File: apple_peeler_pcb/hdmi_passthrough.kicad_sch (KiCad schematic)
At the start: 2 parts, among them U3 4066

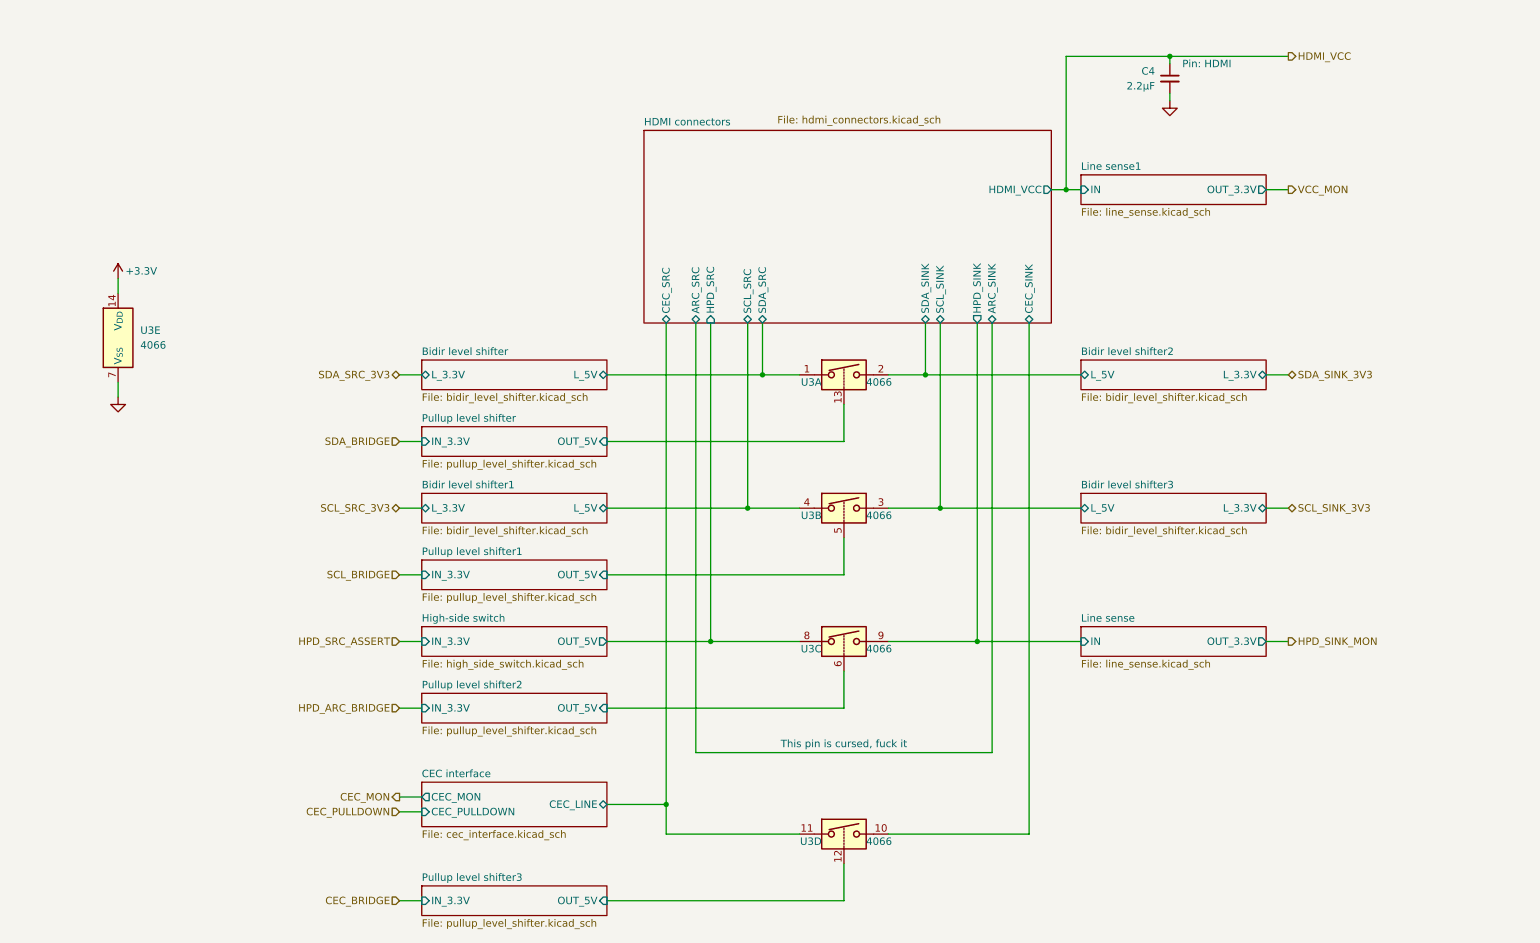
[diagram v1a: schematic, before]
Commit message: we paid for all the pins, we're gonna use all the pins
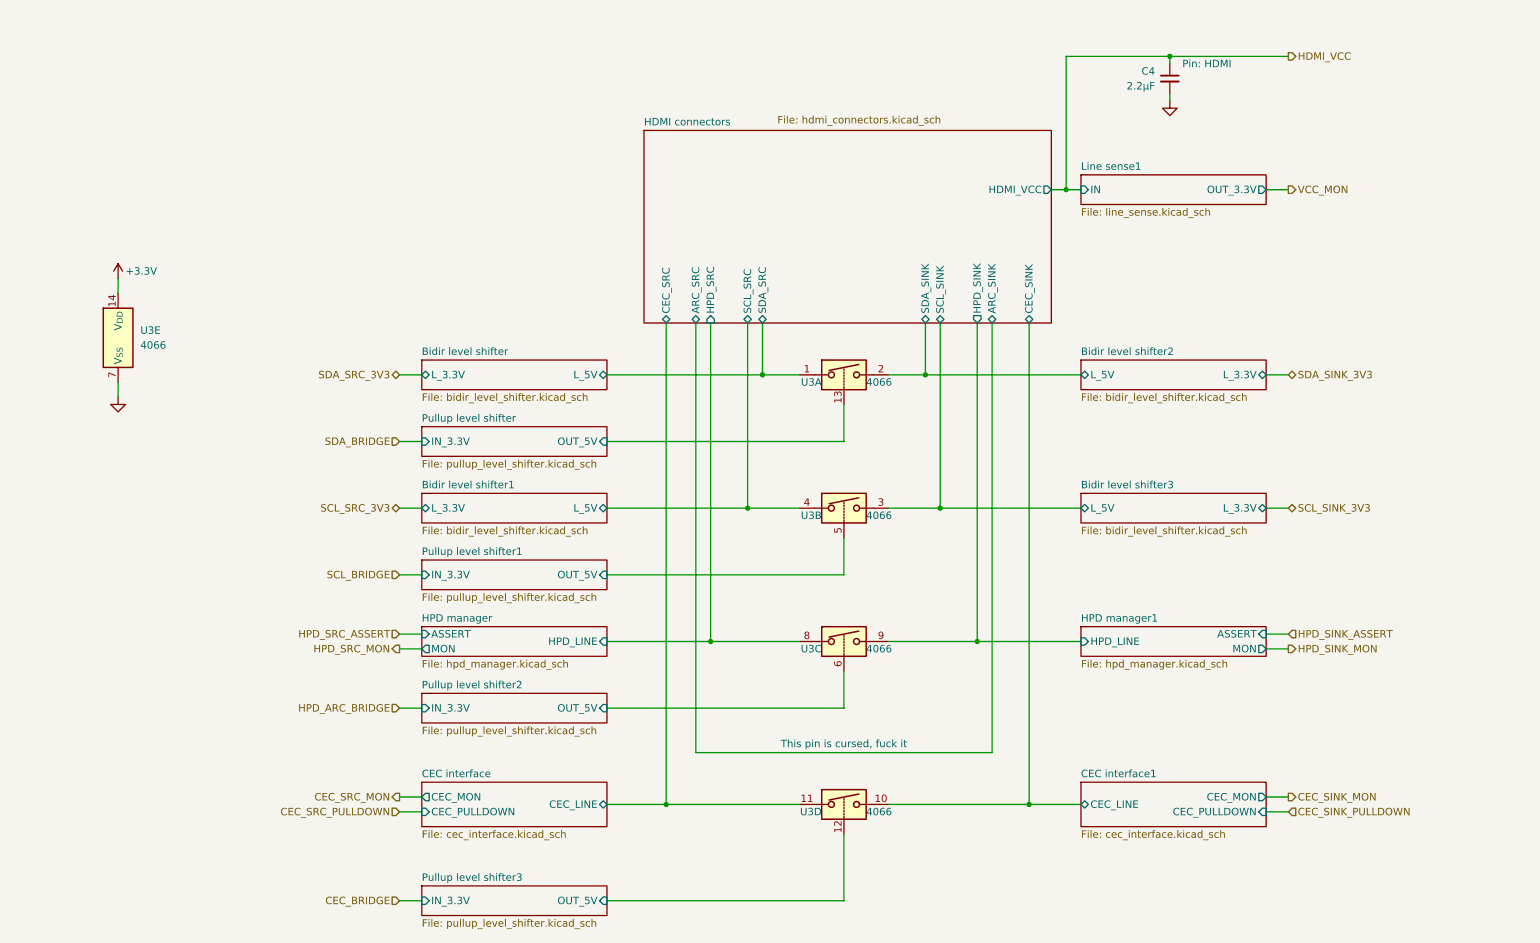
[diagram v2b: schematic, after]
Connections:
- net HDMI connectors/CEC_SINK renamed CEC interface1/CEC_LINE
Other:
- removed sheet High-side switch
- removed sheet Line sense
- added sheet CEC interface1 (cec_interface.kicad_sch)
- added sheet HPD manager (hpd_manager.kicad_sch)
- added sheet HPD manager1 (hpd_manager.kicad_sch)
- moved on the sheet: U3D

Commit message: route hdmi traces
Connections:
- net Bidir level shifter/L_5V: now also U3.11; no longer U3.1
- net Bidir level shifter2/L_5V: now also U3.10; no longer U3.2
- net CEC interface/CEC_LINE: now also U3.1; no longer U3.11
- net CEC interface1/CEC_LINE: now also U3.2; no longer U3.10
- net Pullup level shifter/OUT_5V: now also U3.12; no longer U3.13
- net Pullup level shifter3/OUT_5V: now also U3.13; no longer U3.12
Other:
- moved on the sheet: U3A, U3D
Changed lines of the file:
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@@
 	(symbol
 		(lib_id "Analog_Switch:CD4066BE")
-		(at 162.56 152.4 0)
+		(at 162.56 78.74 0)
 		(unit 4)
 		(exclude_from_sim no)
@@
 		(dnp no)
 		(property "Reference" "U3"
-			(at 158.75 153.67 0)
+			(at 158.75 80.01 0)
 			(effects
 				(font
@@
 		)
 		(property "Value" "4066"
-			(at 166.37 153.67 0)
+			(at 166.37 80.01 0)
 			(effects
 				(font
@@
 		)
 		(property "Footprint" "Package_SO:SO-14_3.9x8.65mm_P1.27mm"
-			(at 162.56 154.94 0)
+			(at 162.56 81.28 0)
 			(effects
 				(font
@@
 		)
 		(property "Datasheet" "https://www.ti.com/lit/ds/symlink/cd4066b.pdf"
-			(at 162.56 152.4 0)
+			(at 162.56 78.74 0)
 			(effects
 				(font
@@
 		)
 		(property "Description" "Quad 20V analog SPST 1:1 switch, DIP-14"
-			(at 162.56 152.4 0)
+			(at 162.56 78.74 0)
 			(effects
 				(font
@@
 		)
 		(property "LCSC" "C512770"
-			(at 162.56 152.4 0)
+			(at 162.56 78.74 0)
 			(effects
 				(font
@@
 		)
 		(property "MPN" "CD4066BM/TR"
-			(at 162.56 152.4 0)
+			(at 162.56 78.74 0)
 			(effects
 				(font
@@
 	(symbol
 		(lib_id "Analog_Switch:CD4066BE")
-		(at 162.56 78.74 0)
+		(at 162.56 152.4 0)
 		(unit 1)
 		(exclude_from_sim no)
@@
 		(dnp no)
 		(property "Reference" "U3"
-			(at 158.75 80.01 0)
+			(at 158.75 153.67 0)
 			(effects
 				(font
@@
 		)
 		(property "Value" "4066"
-			(at 166.37 80.01 0)
+			(at 166.37 153.67 0)
 			(effects
 				(font
@@
 		)
 		(property "Footprint" "Package_SO:SO-14_3.9x8.65mm_P1.27mm"
-			(at 162.56 81.28 0)
+			(at 162.56 154.94 0)
 			(effects
 				(font
@@
 		)
 		(property "Datasheet" "https://www.ti.com/lit/ds/symlink/cd4066b.pdf"
-			(at 162.56 78.74 0)
+			(at 162.56 152.4 0)
 			(effects
 				(font
@@
 		)
 		(property "Description" "Quad 20V analog SPST 1:1 switch, DIP-14"
-			(at 162.56 78.74 0)
+			(at 162.56 152.4 0)
 			(effects
 				(font
@@
 		)
 		(property "LCSC" "C512770"
-			(at 162.56 78.74 0)
+			(at 162.56 152.4 0)
 			(effects
 				(font
@@
 		)
 		(property "MPN" "CD4066BM/TR"
-			(at 162.56 78.74 0)
-			(effects
-				(font
+			(at 162.56 152.4 0)
+			(effects
+				(font

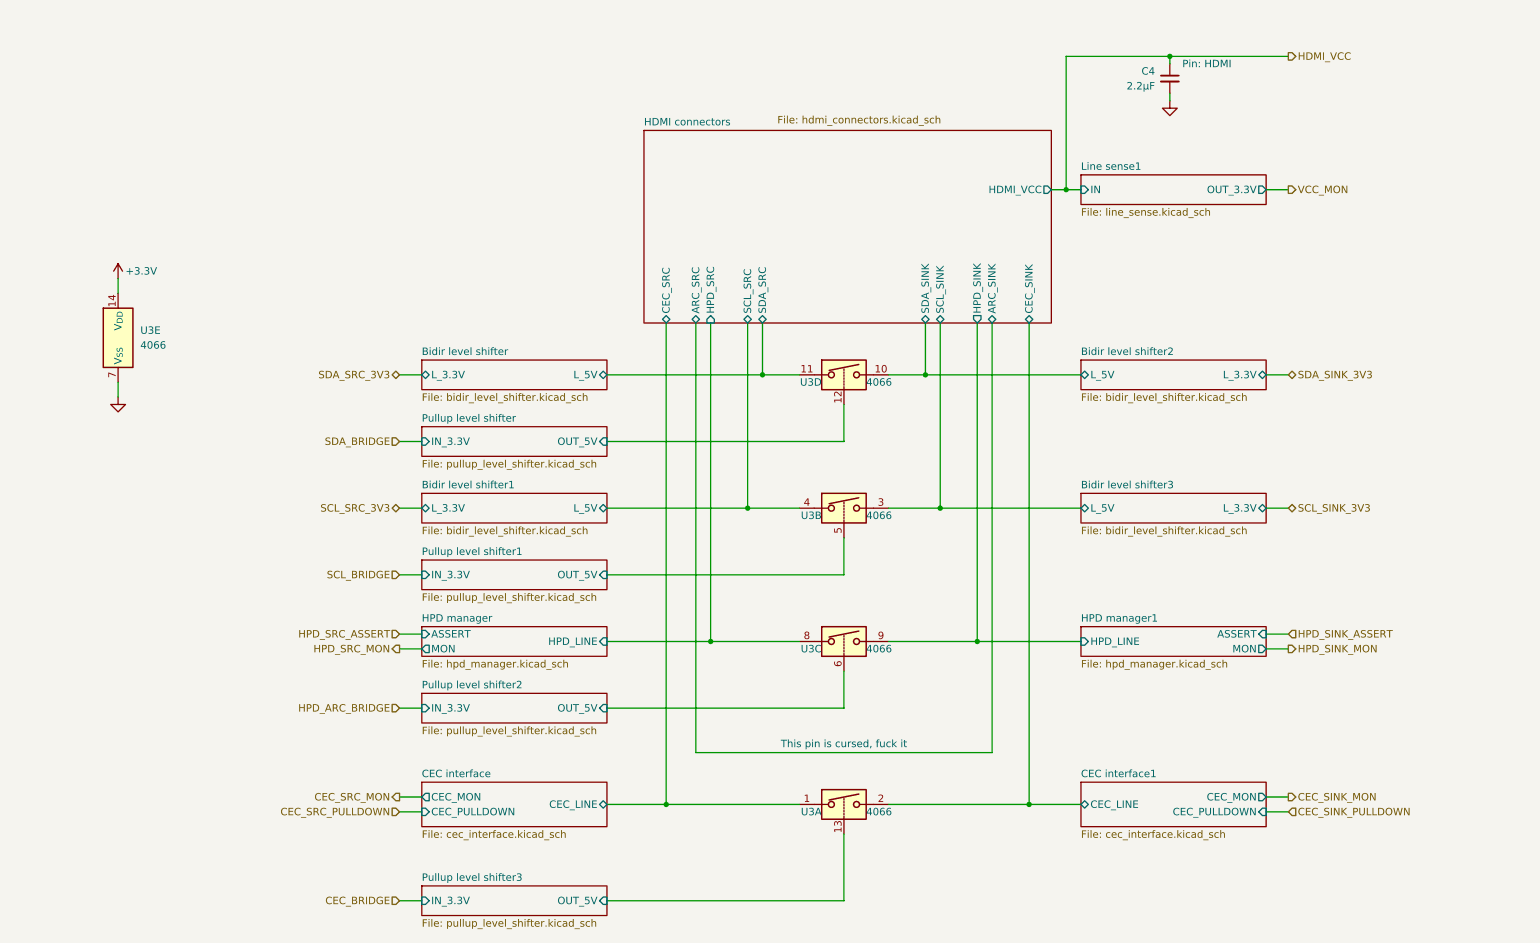
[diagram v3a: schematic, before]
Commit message: sane names for subsheets
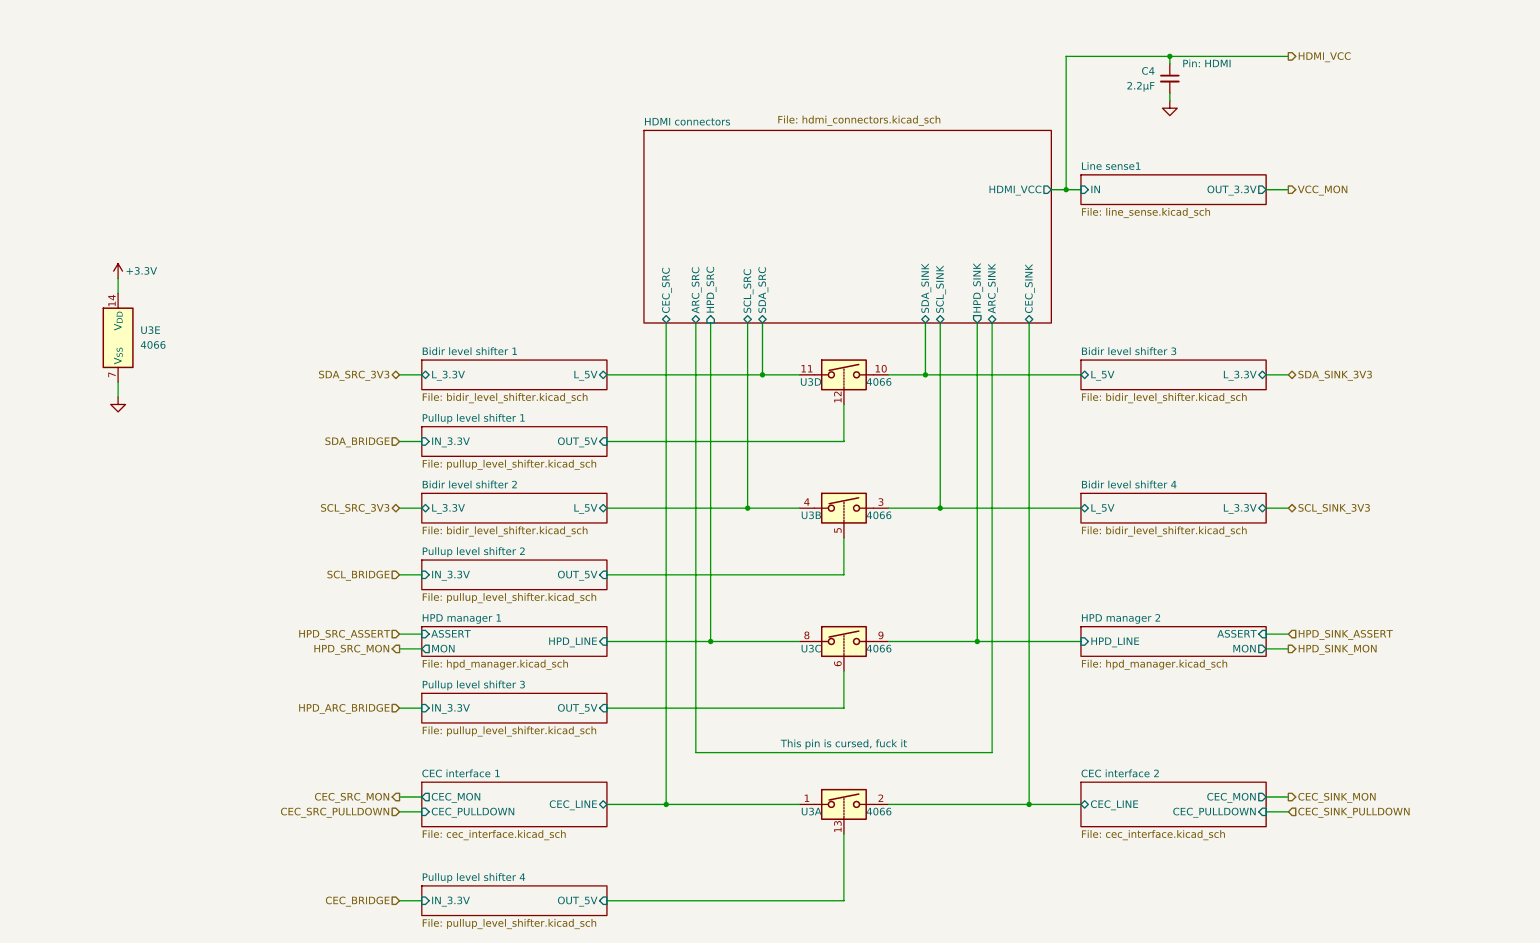
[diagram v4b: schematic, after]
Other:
- sheet Bidir level shifter renamed Bidir level shifter 1
- sheet Bidir level shifter1 renamed Bidir level shifter 2
- sheet Bidir level shifter2 renamed Bidir level shifter 3
- sheet Bidir level shifter3 renamed Bidir level shifter 4
- sheet CEC interface renamed CEC interface 1
- sheet CEC interface1 renamed CEC interface 2
- sheet HPD manager renamed HPD manager 1
- sheet HPD manager1 renamed HPD manager 2
- sheet Pullup level shifter renamed Pullup level shifter 1
- sheet Pullup level shifter1 renamed Pullup level shifter 2
- sheet Pullup level shifter2 renamed Pullup level shifter 3
- sheet Pullup level shifter3 renamed Pullup level shifter 4
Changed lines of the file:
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@@
 			(color 0 0 0 0.0000)
 		)
-		(property "Sheetname" "HPD manager1"
+		(property "Sheetname" "HPD manager 2"
 			(at 203.2 121.2084 0)
 			(effects
@@
 			(color 0 0 0 0.0000)
 		)
-		(property "Sheetname" "HPD manager"
+		(property "Sheetname" "HPD manager 1"
 			(at 90.17 121.2084 0)
 			(effects
@@
 			(color 0 0 0 0.0000)
 		)
-		(property "Sheetname" "Pullup level shifter2"
+		(property "Sheetname" "Pullup level shifter 3"
 			(at 90.17 132.6384 0)
 			(effects
@@
 			(color 0 0 0 0.0000)
 		)
-		(property "Sheetname" "Bidir level shifter1"
+		(property "Sheetname" "Bidir level shifter 2"
 			(at 90.17 98.3484 0)
 			(effects
@@
 			(color 0 0 0 0.0000)
 		)
-		(property "Sheetname" "Pullup level shifter"
+		(property "Sheetname" "Pullup level shifter 1"
 			(at 90.17 86.9184 0)
 			(effects
@@
 			(color 0 0 0 0.0000)
 		)
-		(property "Sheetname" "CEC interface"
+		(property "Sheetname" "CEC interface 1"
 			(at 90.17 147.8784 0)
 			(effects
@@
 			(color 0 0 0 0.0000)
 		)
-		(property "Sheetname" "Pullup level shifter3"
+		(property "Sheetname" "Pullup level shifter 4"
 			(at 90.17 165.6584 0)
 			(effects
@@
 			(color 0 0 0 0.0000)
 		)
-		(property "Sheetname" "CEC interface1"
+		(property "Sheetname" "CEC interface 2"
 			(at 203.2 147.8784 0)
 			(effects
@@
 			(color 0 0 0 0.0000)
 		)
-		(property "Sheetname" "Pullup level shifter1"
+		(property "Sheetname" "Pullup level shifter 2"
 			(at 90.17 109.7784 0)
 			(effects
@@
 			(color 0 0 0 0.0000)
 		)
-		(property "Sheetname" "Bidir level shifter"
+		(property "Sheetname" "Bidir level shifter 1"
 			(at 90.17 75.4884 0)
 			(effects
@@
 			(color 0 0 0 0.0000)
 		)
-		(property "Sheetname" "Bidir level shifter3"
+		(property "Sheetname" "Bidir level shifter 4"
 			(at 203.2 98.3484 0)
 			(effects
@@
 			(color 0 0 0 0.0000)
 		)
-		(property "Sheetname" "Bidir level shifter2"
+		(property "Sheetname" "Bidir level shifter 3"
 			(at 203.2 75.4884 0)
 			(effects

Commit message: rg | xargs sed goes brrr
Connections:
- net HDMI connectors/HPD_SINK renamed HDMI connectors/HPD_B
- net HDMI connectors/HPD_SRC renamed HDMI connectors/HPD_A
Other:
- sheet HDMI connectors ports: added ARC_A, ARC_B, CEC_A, CEC_B, HPD_A, HPD_B, SCL_A, SCL_B, SDA_A, SDA_B; removed ARC_SINK, ARC_SRC, CEC_SINK, CEC_SRC, HPD_SINK, HPD_SRC, SCL_SINK, SCL_SRC, SDA_SINK, SDA_SRC
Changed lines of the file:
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@@
 		)
 	)
-	(hierarchical_label "HPD_SRC_ASSERT"
+	(hierarchical_label "HPD_A_ASSERT"
 		(shape input)
 		(at 86.36 123.19 180)
@@
 		)
 	)
-	(hierarchical_label "CEC_SRC_PULLDOWN"
+	(hierarchical_label "CEC_A_PULLDOWN"
 		(shape input)
 		(at 86.36 153.67 180)
@@
 		)
 	)
-	(hierarchical_label "CEC_SINK_PULLDOWN"
+	(hierarchical_label "CEC_B_PULLDOWN"
 		(shape input)
 		(at 238.76 153.67 0)
@@
 		)
 	)
-	(hierarchical_label "CEC_SRC_MON"
+	(hierarchical_label "CEC_A_MON"
 		(shape output)
 		(at 86.36 151.13 180)
@@
 		)
 	)
-	(hierarchical_label "SCL_SRC_3V3"
+	(hierarchical_label "SCL_A_3V3"
 		(shape bidirectional)
 		(at 86.36 101.6 180)
@@
 		)
 	)
-	(hierarchical_label "SCL_SINK_3V3"
+	(hierarchical_label "SCL_B_3V3"
 		(shape bidirectional)
 		(at 238.76 101.6 0)
@@
 		)
 	)
-	(hierarchical_label "HPD_SINK_MON"
+	(hierarchical_label "HPD_B_MON"
 		(shape output)
 		(at 238.76 125.73 0)
@@
 		)
 	)
-	(hierarchical_label "CEC_SINK_MON"
+	(hierarchical_label "CEC_B_MON"
 		(shape output)
 		(at 238.76 151.13 0)
@@
 		)
 	)
-	(hierarchical_label "SDA_SINK_3V3"
+	(hierarchical_label "SDA_B_3V3"
 		(shape bidirectional)
 		(at 238.76 78.74 0)
@@
 		)
 	)
-	(hierarchical_label "HPD_SRC_MON"
+	(hierarchical_label "HPD_A_MON"
 		(shape output)
 		(at 86.36 125.73 180)
@@
 		)
 	)
-	(hierarchical_label "SDA_SRC_3V3"
+	(hierarchical_label "SDA_A_3V3"
 		(shape bidirectional)
 		(at 86.36 78.74 180)
@@
 		)
 	)
-	(hierarchical_label "HPD_SINK_ASSERT"
+	(hierarchical_label "HPD_B_ASSERT"
 		(shape input)
 		(at 238.76 123.19 0)
@@
 			)
 		)
-		(pin "ARC_SINK" bidirectional
+		(pin "ARC_B" bidirectional
 			(at 187.96 69.85 270)
 			(effects
@@
 			)
 		)
-		(pin "ARC_SRC" bidirectional
+		(pin "ARC_A" bidirectional
 			(at 137.16 69.85 270)
 			(effects
@@
 			)
 		)
-		(pin "CEC_SINK" bidirectional
+		(pin "CEC_B" bidirectional
 			(at 194.31 69.85 270)
 			(effects
@@
 			)
 		)
-		(pin "CEC_SRC" bidirectional
+		(pin "CEC_A" bidirectional
 			(at 132.08 69.85 270)
 			(effects
@@
 			)
 		)
-		(pin "HPD_SINK" output
+		(pin "HPD_B" output
 			(at 185.42 69.85 270)
 			(effects
@@
 			)
 		)
-		(pin "HPD_SRC" input
+		(pin "HPD_A" input
 			(at 139.7 69.85 270)
 			(effects
@@
 			)
 		)
-		(pin "SCL_SINK" bidirectional
+		(pin "SCL_B" bidirectional
 			(at 179.07 69.85 270)
 			(effects
@@
 			)
 		)
-		(pin "SCL_SRC" bidirectional
+		(pin "SCL_A" bidirectional
 			(at 146.05 69.85 270)
 			(effects
@@
 			)
 		)
-		(pin "SDA_SINK" bidirectional
+		(pin "SDA_B" bidirectional
 			(at 176.53 69.85 270)
 			(effects
@@
 			)
 		)
-		(pin "SDA_SRC" bidirectional
+		(pin "SDA_A" bidirectional
 			(at 148.59 69.85 270)
 			(effects
